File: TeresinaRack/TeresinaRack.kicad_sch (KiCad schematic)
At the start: 198 parts, among them J3 USB_Micro-B, J4 SWD, J5 PATCH_SM_EDGE, Q1 MMBT3904, Q2 MMBT3904, SW1 RESET, SW2 BOOT, U1 STM32H750IBK6, U12 TL074, U13 MCP6004, U14 MCP6004, U15 MCP6004, U16 LM4040DBZ-10, U2 IS25LP064A, U3 AS4C16M32MSA-6BIN, U4 PCM3060, U6 TPS62170DSGR, U7 LD1117S50, U8 USBLC6-2SC6, Y1 16MHz

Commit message: PCB: 10-layer re-route with solid GND/+3V3 planes; validation fixes
- 10 layers: In1 solid GND, In6 solid +3V3 (zero traces on either), 8 signal layers
- FMC_A4 routed on In7; GND stitching + USB return vias; fiducials 3xF 1xB
- Schematic: LCSC/MPN part numbers on all parts; removed 13 orphan labels/wires
  (netlist verified identical); ERC/DRC clean; analog paths SPICE-verified
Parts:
- C1, C10, C102, C105, C112, C113, C140, C141, C142, C143, C16, C18, C19, C2, C20, C21, C22, C23, C24, C25, C26, C29, C3, C30, C31, C32, C39, C4, C44, C5, C51, C53, C57, C59, C6, C61, C63, C7, C8, C9: LCSC (none) -> C1525; MPN (none) -> CL05B104KO5NNNC
- C100, C103: LCSC (none) -> C45783; MPN (none) -> CL21A226MAQNNNE
- C101, C104, C126, C127, C128, C129, C130, C131, C132, C133: LCSC (none) -> C1530; MPN (none) -> 0402B221K500NT
- C11, C12, C27, C28: LCSC (none) -> C1779; MPN (none) -> CL21A475KAQNNNE
- C120, C122, C123, C125, C37, C38: LCSC (none) -> C1549; MPN (none) -> 0402CG180J500NT
- C121, C124: LCSC (none) -> C1546; MPN (none) -> 0402CG101J500NT
- C13, C14, C50: LCSC (none) -> C59461; MPN (none) -> CL10A226MQ8NRNC
- C134, C135, C136, C137, C138, C139: LCSC (none) -> C1523; MPN (none) -> 0402B102K500NT
- C15, C17, C48: LCSC (none) -> C52923; MPN (none) -> CL05A105KA5NQNC
- C34, C35, C45, C47, C52, C54, C55, C60, C62: LCSC (none) -> C15850; MPN (none) -> CL21A106KAYNNNE
- C36, C46: LCSC (none) -> C98190; MPN (none) -> CL21A226MOQNNNE
- C56, C58: LCSC (none) -> C12891; MPN (none) -> CL31A226KAHNNNE
- D1, D2, D5: LCSC (none) -> C116953; MPN (none) -> NSR1020MW2T1G
- D3: LCSC (none) -> C965805; MPN (none) -> XL-1608SYGC-06
- D4: LCSC (none) -> C2286; MPN (none) -> KT-0603R
- FB1, FB2: LCSC (none) -> C559338; MPN (none) -> MCR03EZPFX3600
- FB3, FB5, FB7, FB8: LCSC (none) -> C175716; MPN (none) -> CR0805FR600P05Z
- J4: LCSC (none) -> C5151848; MPN (none) -> SWD062R08E8T
- L1: LCSC (none) -> C250233; MPN (none) -> NLCV32T-220K-EF
- Q1, Q2: LCSC (none) -> C20526; MPN (none) -> MMBT3904(RANGE:100-300)
- R1, R2: LCSC (none) -> C25900; MPN (none) -> 0402WGF4701TCE
- R100, R103, R111, R114, R118, R121: LCSC (none) -> C327329; MPN (none) -> RC0402FR-0766K5L
- R101, R104, R13: LCSC (none) -> C25756; MPN (none) -> 0402WGF1502TCE
- R102, R105, R14, R148, R149, R15, R150, R151, R152, R153, R162, R163: LCSC (none) -> C11702; MPN (none) -> 0402WGF1001TCE
- R110, R113, R117, R120: LCSC (none) -> C25762; MPN (none) -> 0402WGF1802TCE
- R112, R115, R119, R122: LCSC (none) -> C25783; MPN (none) -> 0402WGF3902TCE
- R116, R123, R158, R159: LCSC (none) -> C106232; MPN (none) -> RC0402FR-07100RL
- R12: LCSC (none) -> C25792; MPN (none) -> 0402WGF4702TCE
- R124, R125, R126, R127, R128, R129, R130, R131, R154, R155, R160, R161, R164, R165, R166, R167, R168, R169: LCSC (none) -> C25741; MPN (none) -> 0402WGF1003TCE
- R132, R133, R134, R135, R136, R137, R138, R139: LCSC (none) -> C25764; MPN (none) -> 0402WGF2003TCE
- R140, R141, R142, R143, R144, R145, R146, R147: LCSC (none) -> C25779; MPN (none) -> 0402WGF3302TCE
- R170: LCSC (none) -> C4109; MPN (none) -> 0402WGF2001TCE
- R21, R3, R4: LCSC (none) -> C25744; MPN (none) -> 0402WGF1002TCE
- U12: LCSC (none) -> C107644; MPN (none) -> TL074IDT
- U13, U14, U15: LCSC (none) -> C7378; MPN (none) -> MCP6004T-I/SL
- U16: LCSC (none) -> C460604; MPN (none) -> LM4040B30FTA
- U4: LCSC (none) -> C2651841; MPN (none) -> PCM3060PWR
- U7: LCSC (none) -> C81157; MPN (none) -> LD1117S50CTR
- Y1: LCSC (none) -> C13738; MPN (none) -> X322516MLB4SI

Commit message: Patch SM compatibility fixes from deep audit vs official sources
- USB: micro-USB moved to PA11/PA12 (OTG_FS, ROM DFU) with USBLC6; edge pads
  A8/A9 direct to PB14/15 (OTG_HS) per official Rev3 schematic
- PG3 boot strap added (R201 4K7 + C201 2.2uF into BOOT0) for software DFU
- CV-out gain resistors to official 120K/62K (51.5k unavailable at JLC)
- QSPI_NCS flash leg re-routed via In8; routing artifacts cleaned
- BOM 100% LCSC-resolved; silk name/rev; USB/boot 0.09mm rule (.kicad_dru)
- DRC 0 errors, 0 unconnected; planes solid; SPICE 59/59
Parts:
- added C201: 2.2uF, Capacitor_SMD:C_0603_1608Metric, symbol Device:C
- added R201: 4K7, Resistor_SMD:R_0402_1005Metric, symbol Device:R
- R11: LCSC (none) -> C25128; MPN (none) -> 0402WGF510KTCE
- R154, R155: value 100K -> 120K; LCSC C25741 -> C25750; MPN 0402WGF1003TCE -> 0402WGF1203TCE
- R156, R157: value 51K5 -> 62K; LCSC (none) -> C2909375; MPN (none) -> FRC0402F6202TS
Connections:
- net BOOT0: now also C201.1, R201.2
- net GND: now also C201.2
- net USB_DM: no longer J3.2 (D-), U8.1 (I/O1), U8.6 (I/O1)
- net USB_DP: no longer J3.3 (D+), U8.3 (I/O2), U8.4 (I/O2)
- net USB_FS_DP: now reaches U1.B15 (PA12)
- net USB_FS_DP: now also J3.3 (D+), U8.3 (I/O2), U8.4 (I/O2)
- net USB_FS_DM: now reaches U1.C15 (PA11)
- net USB_FS_DM: now also J3.2 (D-), U8.1 (I/O1), U8.6 (I/O1)
- net BOOT_FLASH: now reaches U1.K15 (PG3)
- net BOOT_FLASH: now also R201.1

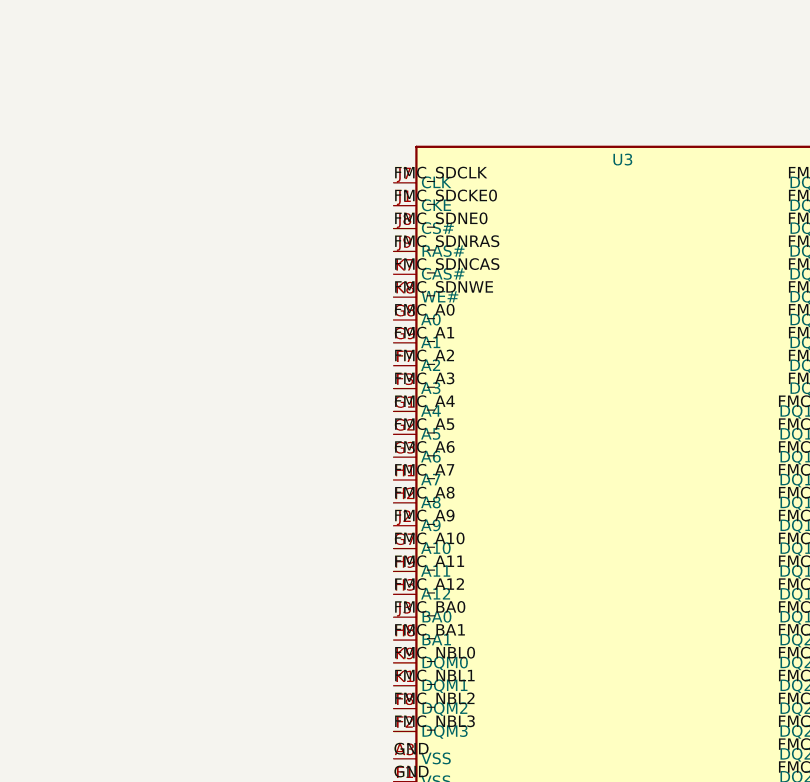
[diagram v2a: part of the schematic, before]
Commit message: Fix critical SDRAM symbol bug; reroute on 12 layers
The custom AS4C16M32MSA symbol (shared with the Teresina board) had 5
control/address balls scrambled vs the Alliance Memory datasheet: CLK, CKE,
BA0, A2, A9 were assigned to the wrong balls (a single 5-cycle in the J row),
which would leave the 64 MB SDRAM dead on every board. This was invisible to
the earlier audit because every check compared the board against this (wrong)
symbol. Corrected the ball numbers in TeresinaRack.kicad_sym and the cached
copy in .kicad_sch; the flash IS25LP064A symbol was audited and is correct.

The 5 corrected nets could not be rerouted on the 10-layer board (the STM32's
0.65 mm-pitch BGA escape cannot fit 5 permuted nets in the residual space, and
freerouting 2.2.4 crashes on this DSN). Grew the board to 12 layers (added
In9/In10 signal) and routed all 5 with via-in-pad at each ball + In9/In10 at
full 0.1 mm clearance. Verified: DRC-neutral (0 violations added), 0 unrouted
ratsnest, ERC unchanged, all 5 nets on the datasheet-correct balls. Regenerated
the 12-layer fab package; updated README stackup and via count.
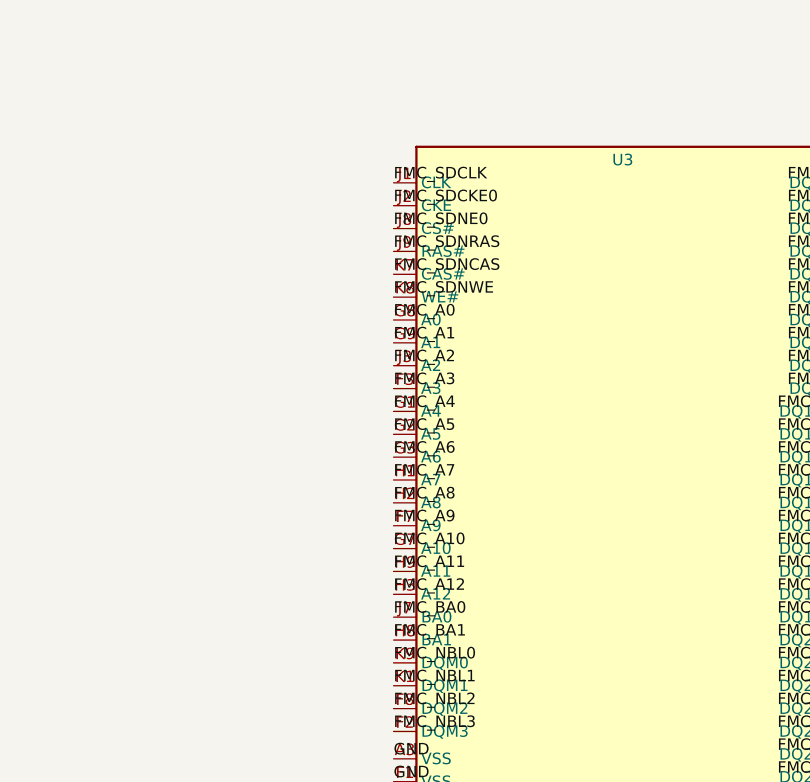
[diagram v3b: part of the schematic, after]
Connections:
- net FMC_A2: now also U3.J3 (A2); no longer U3.F7 (A2)
- net FMC_A9: now also U3.F7 (A9); no longer U3.J2 (A9)
- net FMC_BA0: now also U3.J7 (BA0); no longer U3.J3 (BA0)
- net FMC_SDCKE0: now also U3.J2 (CKE); no longer U3.J1 (CKE)
- net FMC_SDCLK: now also U3.J1 (CLK); no longer U3.J7 (CLK)

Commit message: Match official Rev3: audio MFB cap placement + gate-in collector pull-up
Evidence-based re-audit against the official Patch SM Rev3 confirmed the board
is a faithful copy (symbols all match datasheets, analog blocks part-for-part).
Corrected two deviations toward the official design:

- Audio output MFB filter: moved the 18 pF feedback cap (C120/C123) from across
  the 39K T-branch to the op-amp inverting input -- the canonical MFB placement,
  restoring codec-to-single-ended CMRR and phase margin. Schematic relabelled and
  the two nets rerouted on the audio layers; 0 unconnected, DRC unchanged.
- Gate-in collector pull-up 100K -> 10K (R168/R169, LCSC C72443) to match official
  and stay robust if firmware enables an internal pull-down on PG13/PG14.

Also merged a duplicate USB_FS_DM via (cleared the lone hole_to_hole DFM flag) and
fixed a README claim (120K/62K is the official CV-out value, not a 51.5K substitution).
Remaining gate-in base-pulldown (100K vs 1M) / omitted series-R and the gate-out
comparator topology are documented, benign deviations. Regenerated 12-layer fab.
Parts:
- R168, R169: value 100K -> 10K; LCSC C25741 -> C72443
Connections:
- net N_OLA: no longer C120.2, C121.1
- net N_ORA: no longer C123.2, C124.1
- net OL_INV: now also C120.2, C121.1
- net OR_INV: now also C123.2, C124.1
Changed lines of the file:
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@@
 		)
 	)
-	(label "N_OLA"
+	(label "OL_INV"
 		(at 770.0 488.81 90)
 		(effects
@@
 		)
 	)
-	(label "N_ORA"
+	(label "OR_INV"
 		(at 830.0 488.81 90)
 		(effects
@@
 			)
 		)
-		(property "Value" "100K"
+		(property "Value" "10K"
 			(at 1342.16 567.42 0)
 			(show_name no)
@@
 			)
 		)
-		(property "LCSC" "C25741" (at 0 0 0)
+		(property "LCSC" "C72443" (at 0 0 0)
 			(effects
 				(font
@@
 			)
 		)
-		(property "Value" "100K"
+		(property "Value" "10K"
 			(at 1477.16 567.42 0)
 			(show_name no)
@@
 			)
 		)
-		(property "LCSC" "C25741" (at 0 0 0)
+		(property "LCSC" "C72443" (at 0 0 0)
 			(effects
 				(font

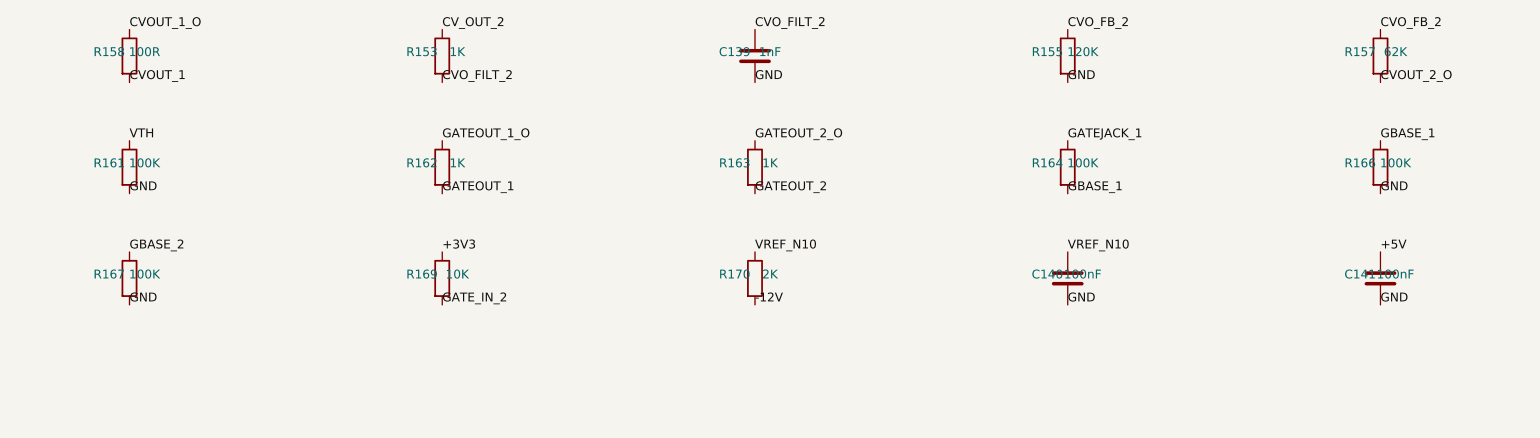
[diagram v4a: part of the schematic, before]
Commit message: Gate-in base pull-down 100K->1M (R166/R167, LCSC C26083)
Completes the gate-in value match to the official Rev3: base pull-down set to
the official 1M (verified UNI-ROYAL 0402WGF1004TCE = LCSC C26083, in stock at
JLCPCB). Schematic value+LCSC and PCB value updated. Metadata-only (no copper
change); DRC/ERC unchanged.
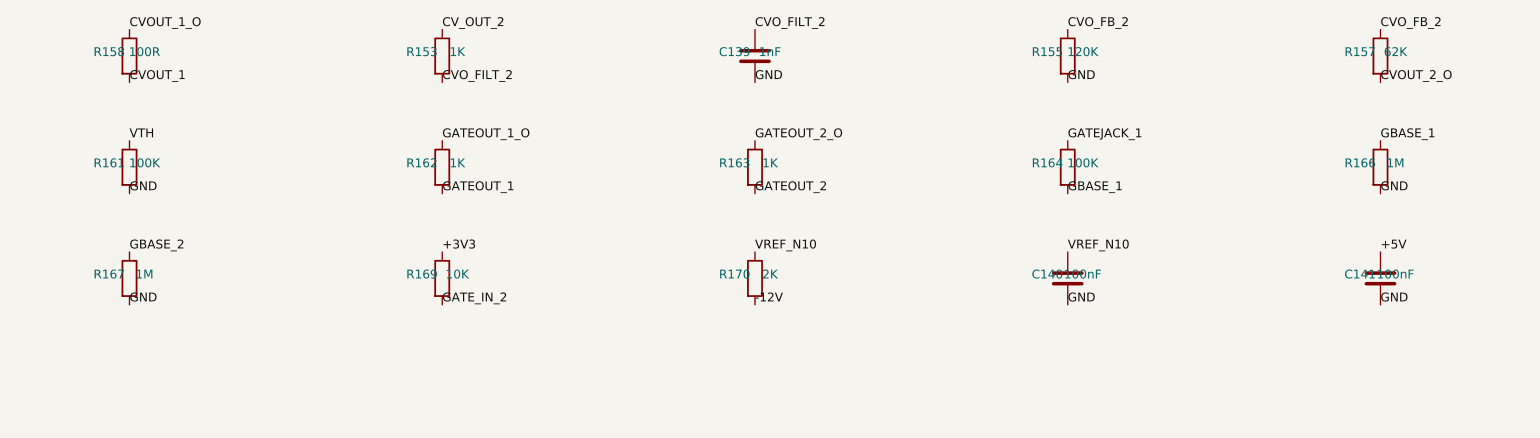
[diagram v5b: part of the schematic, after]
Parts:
- R166, R167: value 100K -> 1M; LCSC C25741 -> C26083
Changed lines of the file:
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@@
 			)
 		)
-		(property "Value" "100K"
+		(property "Value" "1M"
 			(at 1612.16 551.42 0)
 			(show_name no)
@@
 			)
 		)
-		(property "LCSC" "C25741" (at 0 0 0)
+		(property "LCSC" "C26083" (at 0 0 0)
 			(effects
 				(font
@@
 			)
 		)
-		(property "Value" "100K"
+		(property "Value" "1M"
 			(at 1432.16 567.42 0)
 			(show_name no)
@@
 			)
 		)
-		(property "LCSC" "C25741" (at 0 0 0)
-			(effects
-				(font
+		(property "LCSC" "C26083" (at 0 0 0)
+			(effects
+				(font

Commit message: Add gate-in 1K series resistors; fix latent audio bridge-cap and sourcing bugs
- Gate-in 1K collector series R (R202/R203) into PG13/PG14, matching official Rev3
- Fix C121/C124 MFB bridge caps mis-wired to *_INV in schematic (should be N_OxA junctions)
- Correct stale LCSC/MPN on R166-169 (100K->1M/10K parts) and set R202/R203 (1K)
- README: 201 parts/51 groups/825 vias; deviations rewritten
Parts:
- added R202, R203: 1K, Resistor_SMD:R_0402_1005Metric, symbol Device:R
- R166, R167: MPN 0402WGF1003TCE -> 0402WGF1004TCE
- R168, R169: MPN 0402WGF1003TCE -> 0402WGF1002TCE
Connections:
- net GATE_IN_1: now also R202.1; no longer U1.A8 (PG13)
- net GATE_IN_2: now also R203.1; no longer U1.A7 (PG14)
- net N_OLA: now also C121.1
- net N_ORA: now also C124.1
- net OL_INV: no longer C121.1
- net OR_INV: no longer C124.1
- new net GATE_IN_1_MCU: R202.2, U1.A8 (PG13)
- new net GATE_IN_2_MCU: R203.2, U1.A7 (PG14)

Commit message: Fix critical PCM3060 analog supply (audio) + LM4040 reference sourcing
Forensic audio audit vs official Rev3 + full kicad-happy suite.

- Codec V_CC (U4.24) was on +3V3A (3.3V); PCM3060 datasheet requires 4.5-5.5V
  analog. Added ferrite-filtered +5VA rail (FB9 + C202 100nF + C203 10uF) to
  pin 24 -> correct VCOM (2.5V) and full-scale audio. PWR_FLAG on +5VA.
- U16 LM4040: value was 10V but MPN/LCSC pointed to a 3.0V part
  (LM4040B30/C460604); corrected to LM4040C10IDBZR / C201738 (10V).
- DRC 0 shorts / 0 unconnected; ERC 3 pre-existing benign; SPICE 63/63.
- README: codec-supply fix, +5VA rail, 204 parts / 829 vias.
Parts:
- added C202: 100nF, Capacitor_SMD:C_0402_1005Metric, symbol Device:C
- added C203: 10uF, Capacitor_SMD:C_0805_2012Metric, symbol Device:C
- added FB9: 600R@100MHz, Inductor_SMD:L_0805_2012Metric, symbol Device:FerriteBead
- U16: LCSC C460604 -> C201738; MPN LM4040B30FTA -> LM4040C10IDBZR
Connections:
- net +3V3A: no longer U4.24 (V_{CC})
- net +5V: now also FB9.1
- net GND: now also C202.2, C203.2
- new net +5VA: C202.1, C203.1, FB9.2, U4.24 (V_{CC})

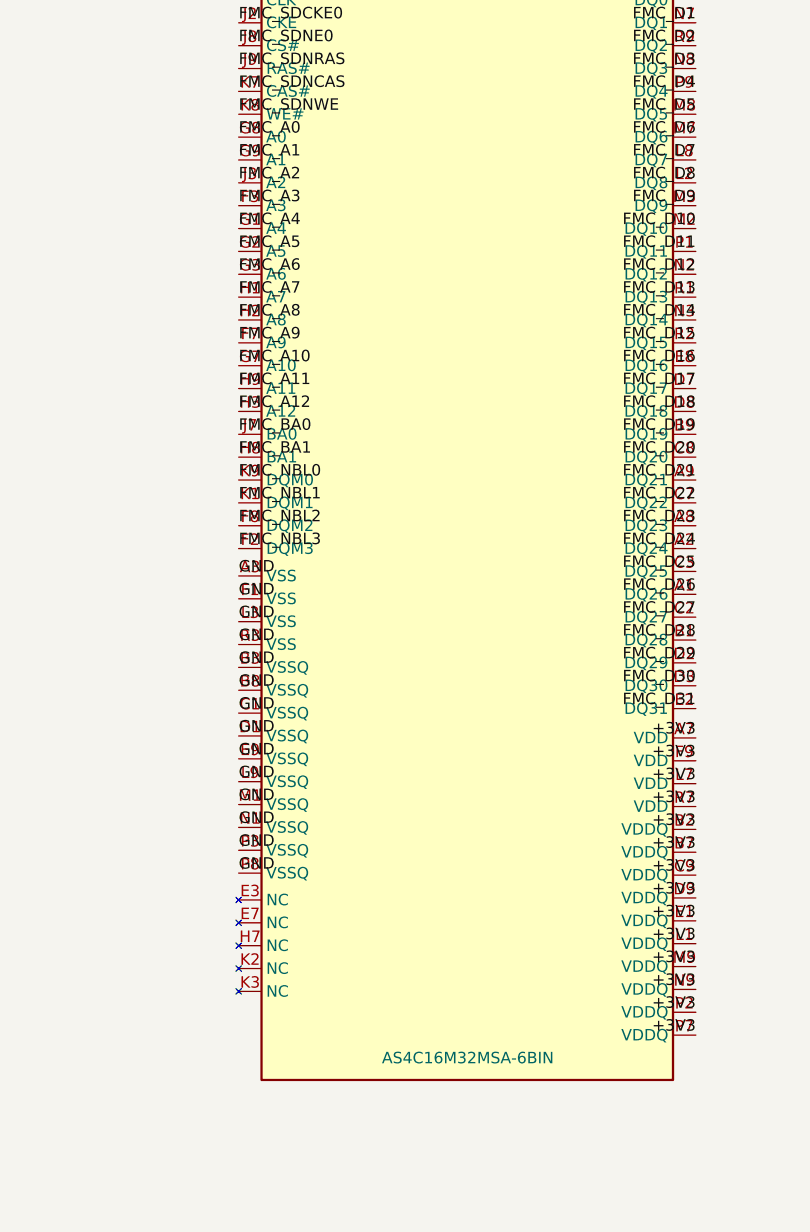
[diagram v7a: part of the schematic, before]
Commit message: Fix SDRAM A2/A9 ball swap; switch SDRAM to ISSI IS42S32160F
- A2/A9 address lines were swapped at U3 (ball J3 must=A9, F7 must=A2
  per datasheet); corrected symbol pin numbers + rerouted FMC_A2/FMC_A9.
- SDRAM -> ISSI IS42S32160F-6BLI (LCSC C1348852): native 3.3V, JLC-stocked,
  ball-map identical to AS4C16M32, libDaisy-compatible. Alliance MSA was a
  1.8V mobile part run out-of-spec and not orderable at JLC.
- README/BOM sourcing notes corrected.
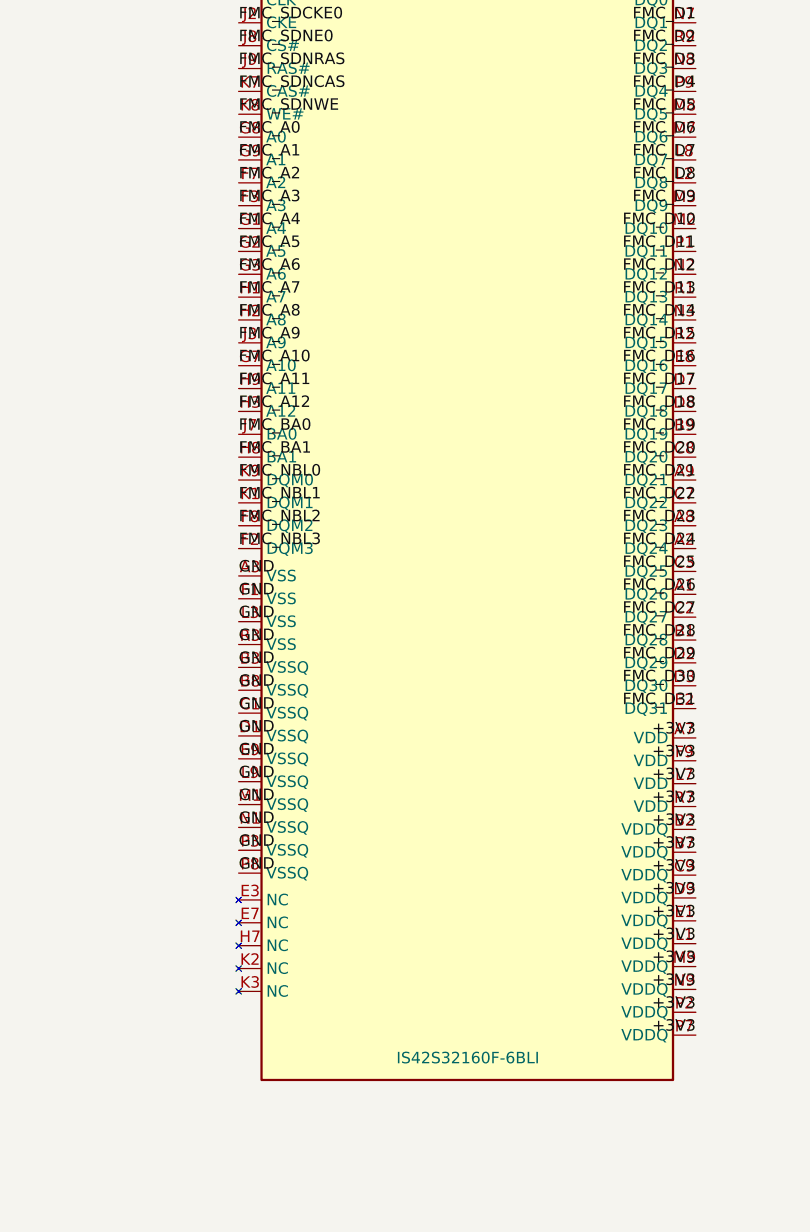
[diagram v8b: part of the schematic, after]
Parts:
- U3: value AS4C16M32MSA-6BIN -> IS42S32160F-6BLI; LCSC TBD-verify-stock -> C1348852; MPN AS4C16M32MSA-6BIN -> IS42S32160F-6BLI
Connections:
- net FMC_A2: now also U3.F7 (A2); no longer U3.J3 (A2)
- net FMC_A9: now also U3.J3 (A9); no longer U3.F7 (A9)
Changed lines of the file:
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@@
 			)
 		)
-		(property "Value" "AS4C16M32MSA-6BIN"
+		(property "Value" "IS42S32160F-6BLI"
 			(at 560.07 209.56 0)
 			(show_name no)
@@
 			)
 		)
-		(property "Datasheet" "https://www.alliancememory.com/wp-content/uploads/pdf/mobile_sdram/20171206_AllianceMemory_512M_LPSDRAM_AS4C16M32MSA-6BIN(TR)_rev1.0_Dec2017.pdf"
+		(property "Datasheet" "https://www.issi.com/WW/pdf/42-45S32160F.pdf"
 			(at 560 142.38 0)
 			(hide yes)
@@
 			)
 		)
-		(property "Description" "512Mb (16M x 32) Mobile LP-SDRAM, 166MHz, 90-ball FBGA (8x13mm). NOTE: nominal 1.8V part."
+		(property "Description" "512Mb (16M x 32) SDRAM, 3.3V, 166MHz, 90-ball FBGA (8x13mm) — JEDEC ballmap (AS4C16M32 / IS42S32160 compatible)."
 			(at 560 139.84 0)
 			(hide yes)
@@
 			)
 		)
-		(property "MPN" "AS4C16M32MSA-6BIN"
+		(property "MPN" "IS42S32160F-6BLI"
 			(at 560.0 150.0 0)
 			(effects
@@
 			)
 		)
-		(property "LCSC" "TBD-verify-stock"
+		(property "LCSC" "C1348852"
 			(at 560.0 150.0 0)
 			(effects
